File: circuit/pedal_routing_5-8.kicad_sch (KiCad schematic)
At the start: 12 parts, among them U23 CD4051B, U24 CD4051B, U25 CD4051B, U26 CD4051B

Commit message: Created pdf and made minor readabilty changes.
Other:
- title: ESP332 Guitar Patch Bay -> (none)
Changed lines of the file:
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@@
 	(generator "eeschema")
 	(generator_version "9.0")
-	(paper "USLetter")
-	(title_block
-		(title "ESP332 Guitar Patch Bay")
-		(date "2025-05-27")
-		(rev "1")
-	)
+	(paper "A4")
 	(text "Pedal 8 Routing"
 		(exclude_from_sim no)

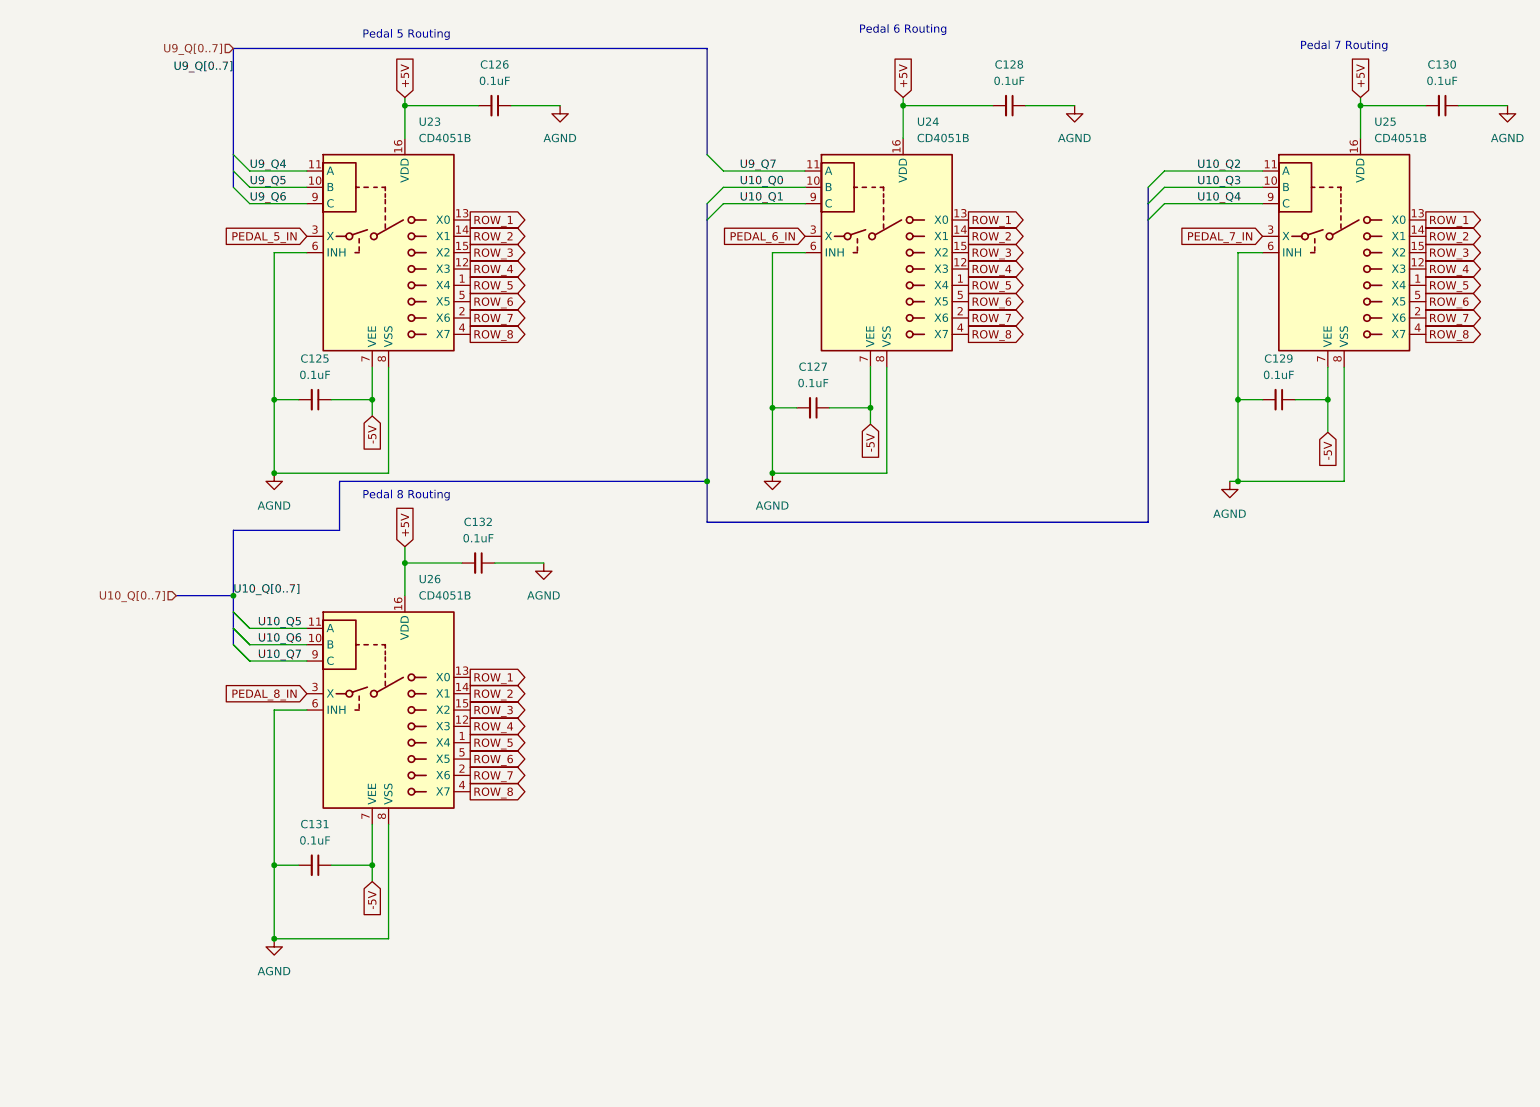
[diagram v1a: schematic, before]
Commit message: Rebuilt Matrix and added inhibit function.
Matrix was flawed, It now supports 8 FX loops (pedals) in any order. Or optionally none at all with a buffered bypass, or anywhere in between. The inhibit function will allow the option to press any loop foot switch an enable or disable it without reprogramming.
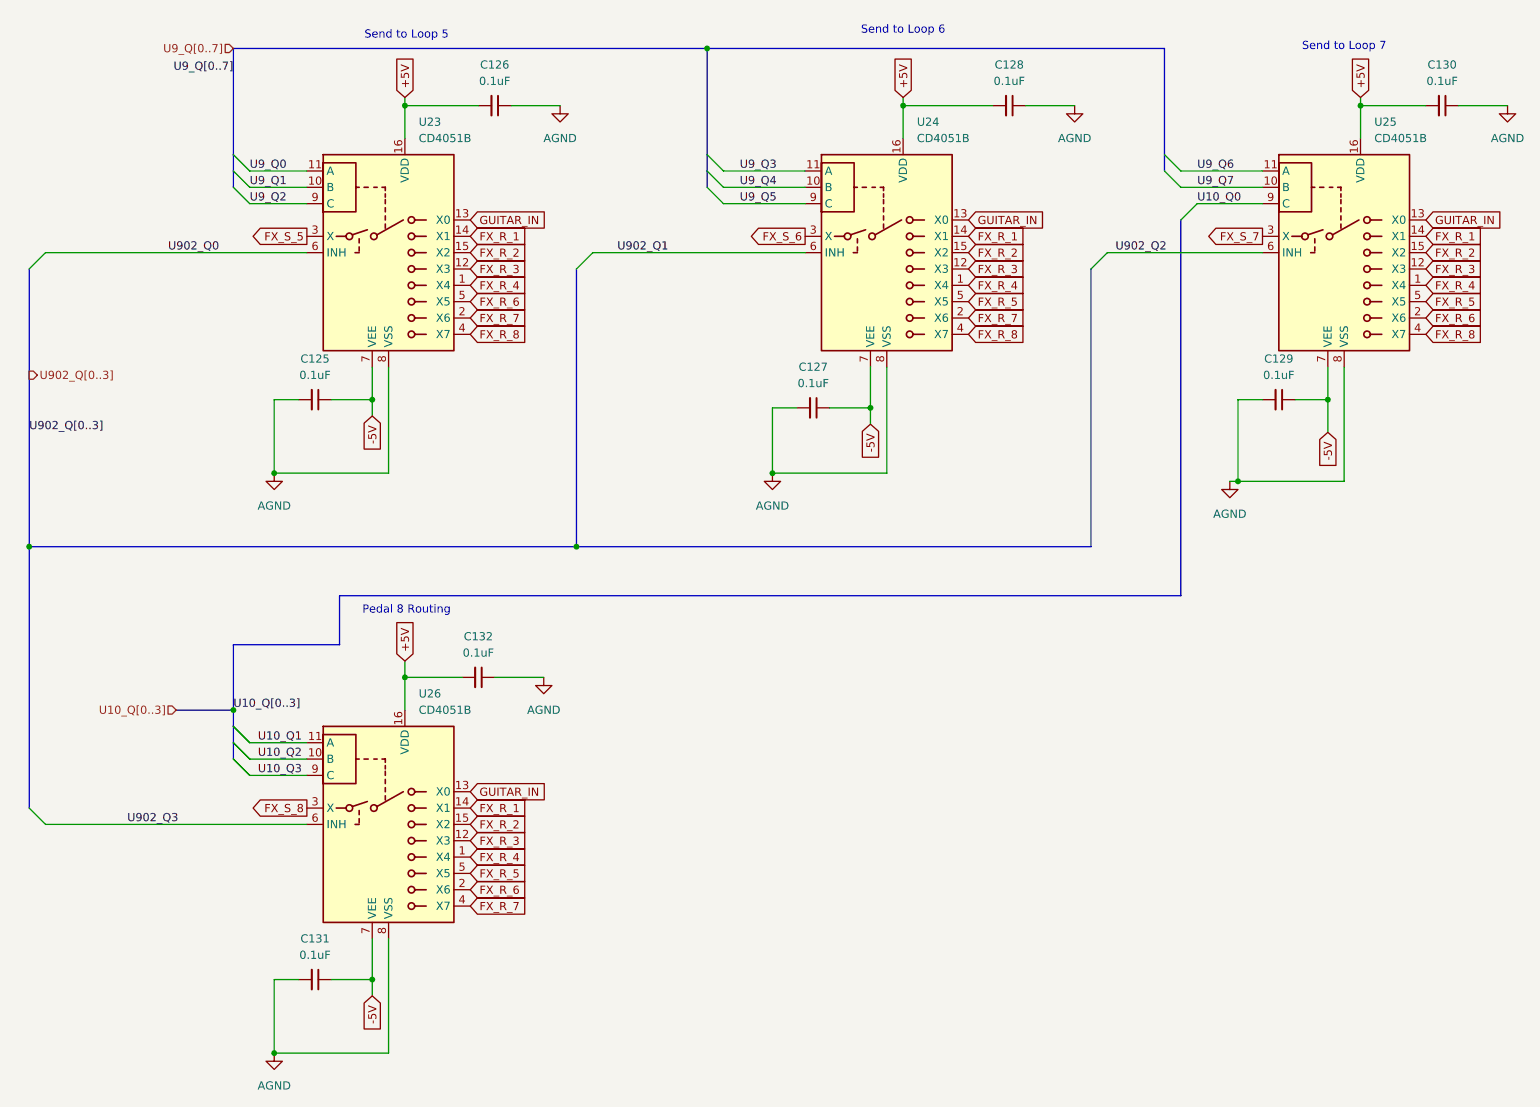
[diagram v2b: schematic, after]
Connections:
- net U10_Q4 is gone; now on net U10_Q0: U25.9 (C)
- net U10_Q5 is gone; now on net U10_Q1: U26.11 (A)
- net U10_Q6 is gone; now on net U10_Q2: U26.10 (B)
- net U10_Q7 is gone; now on net U10_Q3: U26.9 (C)
- net AGND: no longer U23.6 (INH), U24.6 (INH), U25.6 (INH), U26.6 (INH)
- net U10_Q0: no longer U24.10 (B)
- net U10_Q1: no longer U24.9 (C)
- net U10_Q2: no longer U25.11 (A)
- net U10_Q3: no longer U25.10 (B)
- net U9_Q4: now also U24.10 (B); no longer U23.11 (A)
- net U9_Q5: now also U24.9 (C); no longer U23.10 (B)
- net U9_Q6: now also U25.11 (A); no longer U23.9 (C)
- net U9_Q7: now also U25.10 (B); no longer U24.11 (A)
- net PEDAL_5_IN renamed FX_S_5
- net PEDAL_6_IN renamed FX_S_6
- net PEDAL_7_IN renamed FX_S_7
- net PEDAL_8_IN renamed FX_S_8
- net ROW_1 renamed GUITAR_IN
- net ROW_2 renamed FX_R_1
- net ROW_3 renamed FX_R_2
- net ROW_4 renamed FX_R_3
- net ROW_5 renamed FX_R_4
- net ROW_6 renamed FX_R_5
- net FX_R_5: no longer U23.5 (X5)
- net ROW_7 renamed FX_R_6
- net FX_R_6: now also U23.5 (X5); no longer U23.2 (X6), U24.2 (X6)
- net ROW_8 renamed FX_R_8
- net FX_R_8: no longer U26.4 (X7)
- new net FX_R_7: U23.2 (X6), U24.2 (X6), U26.4 (X7)
- new net U902_Q0: U23.6 (INH)
- new net U902_Q1: U24.6 (INH)
- new net U902_Q2: U25.6 (INH)
- new net U902_Q3: U26.6 (INH)
- new net U9_Q0: U23.11 (A)
- new net U9_Q1: U23.10 (B)
- new net U9_Q2: U23.9 (C)
- new net U9_Q3: U24.11 (A)
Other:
- note added: "Send to Loop 5"
- note added: "Send to Loop 6"
- note added: "Send to Loop 7"
- note removed: "Pedal 5 Routing"
- note removed: "Pedal 6 Routing"
- note removed: "Pedal 7 Routing"
- moved on the sheet: C131, C132, U26

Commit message: Re-annotation of circuit, new PCB routing, updated PDF
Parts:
- renumbered C126 to C601, C128 to C602, C130 to C603, C125 to C604, C129 to C605, C127 to C606, C132 to C607, C131 to C608, U23 to U601, U24 to U602, U25 to U603, U26 to U604
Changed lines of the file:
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@@
 		(dnp no)
 		(fields_autoplaced yes)
-		(property "Reference" "U26"
+		(property "Reference" "U604"
 			(at 77.0733 119.38 0)
 			(effects
@@
 			(project "circuit"
 				(path "/420e3d7a-6c9a-4806-b4be-05d56aeb21de/badefe61-f2aa-4ce3-b43f-f44172d96524"
-					(reference "U26")
+					(reference "U604")
 					(unit 1)
 				)
@@
 		(dnp no)
 		(fields_autoplaced yes)
-		(property "Reference" "C130"
+		(property "Reference" "C603"
 			(at 236.2136 21.59 90)
 			(effects
@@
 			(project "circuit"
 				(path "/420e3d7a-6c9a-4806-b4be-05d56aeb21de/badefe61-f2aa-4ce3-b43f-f44172d96524"
-					(reference "C130")
+					(reference "C603")
 					(unit 1)
 				)
@@
 		(on_board yes)
 		(dnp no)
-		(property "Reference" "#PWR0604"
+		(property "Reference" "#PWR0605"
 			(at 132.08 91.44 0)
 			(effects
@@
 			(project "circuit"
 				(path "/420e3d7a-6c9a-4806-b4be-05d56aeb21de/badefe61-f2aa-4ce3-b43f-f44172d96524"
-					(reference "#PWR0604")
+					(reference "#PWR0605")
 					(unit 1)
 				)
@@
 		(on_board yes)
 		(dnp no)
-		(property "Reference" "#PWR0107"
+		(property "Reference" "#PWR0602"
 			(at 179.07 34.29 0)
 			(effects
@@
 			(project "circuit"
 				(path "/420e3d7a-6c9a-4806-b4be-05d56aeb21de/badefe61-f2aa-4ce3-b43f-f44172d96524"
-					(reference "#PWR0107")
+					(reference "#PWR0602")
 					(unit 1)
 				)
@@
 		(dnp no)
 		(fields_autoplaced yes)
-		(property "Reference" "C129"
+		(property "Reference" "C605"
 			(at 210.8136 67.31 90)
 			(effects
@@
 			(project "circuit"
 				(path "/420e3d7a-6c9a-4806-b4be-05d56aeb21de/badefe61-f2aa-4ce3-b43f-f44172d96524"
-					(reference "C129")
+					(reference "C605")
 					(unit 1)
 				)
@@
 		(on_board yes)
 		(dnp no)
-		(property "Reference" "#PWR0601"
+		(property "Reference" "#PWR0604"
 			(at 54.61 91.44 0)
 			(effects
@@
 			(project "circuit"
 				(path "/420e3d7a-6c9a-4806-b4be-05d56aeb21de/badefe61-f2aa-4ce3-b43f-f44172d96524"
-					(reference "#PWR0601")
+					(reference "#PWR0604")
 					(unit 1)
 				)
@@
 		(on_board yes)
 		(dnp no)
-		(property "Reference" "#PWR0106"
+		(property "Reference" "#PWR0601"
 			(at 99.06 34.29 0)
 			(effects
@@
 			(project "circuit"
 				(path "/420e3d7a-6c9a-4806-b4be-05d56aeb21de/badefe61-f2aa-4ce3-b43f-f44172d96524"
-					(reference "#PWR0106")
+					(reference "#PWR0601")
 					(unit 1)
 				)
@@
 		(dnp no)
 		(fields_autoplaced yes)
-		(property "Reference" "C132"
+		(property "Reference" "C607"
 			(at 86.3536 110.49 90)
 			(effects
@@
 			(project "circuit"
 				(path "/420e3d7a-6c9a-4806-b4be-05d56aeb21de/badefe61-f2aa-4ce3-b43f-f44172d96524"
-					(reference "C132")
+					(reference "C607")
 					(unit 1)
 				)
@@
 		(dnp no)
 		(fields_autoplaced yes)
-		(property "Reference" "C131"
+		(property "Reference" "C608"
 			(at 60.9536 157.48 90)
 			(effects
@@
 			(project "circuit"
 				(path "/420e3d7a-6c9a-4806-b4be-05d56aeb21de/badefe61-f2aa-4ce3-b43f-f44172d96524"
-					(reference "C131")
+					(reference "C608")
 					(unit 1)
 				)
@@
 		(dnp no)
 		(fields_autoplaced yes)
-		(property "Reference" "C127"
+		(property "Reference" "C606"
 			(at 138.4236 68.58 90)
 			(effects
@@
 			(project "circuit"
 				(path "/420e3d7a-6c9a-4806-b4be-05d56aeb21de/badefe61-f2aa-4ce3-b43f-f44172d96524"
-					(reference "C127")
+					(reference "C606")
 					(unit 1)
 				)
@@
 		(on_board yes)
 		(dnp no)
-		(property "Reference" "#PWR0108"
+		(property "Reference" "#PWR0603"
 			(at 246.38 34.29 0)
 			(effects
@@
 			(project "circuit"
 				(path "/420e3d7a-6c9a-4806-b4be-05d56aeb21de/badefe61-f2aa-4ce3-b43f-f44172d96524"
-					(reference "#PWR0108")
+					(reference "#PWR0603")
 					(unit 1)
 				)
@@
 		(dnp no)
 		(fields_autoplaced yes)
-		(property "Reference" "C126"
+		(property "Reference" "C601"
 			(at 88.8936 21.59 90)
 			(effects
@@
 			(project "circuit"
 				(path "/420e3d7a-6c9a-4806-b4be-05d56aeb21de/badefe61-f2aa-4ce3-b43f-f44172d96524"
-					(reference "C126")
+					(reference "C601")
 					(unit 1)
 				)
@@
 		(on_board yes)
 		(dnp no)
-		(property "Reference" "#PWR0603"
+		(property "Reference" "#PWR0606"
 			(at 203.2 92.71 0)
 			(effects
@@
 			(project "circuit"
 				(path "/420e3d7a-6c9a-4806-b4be-05d56aeb21de/badefe61-f2aa-4ce3-b43f-f44172d96524"
-					(reference "#PWR0603")
+					(reference "#PWR0606")
 					(unit 1)
 				)
@@
 		(dnp no)
 		(fields_autoplaced yes)
-		(property "Reference" "C128"
+		(property "Reference" "C602"
 			(at 168.9036 21.59 90)
 			(effects
@@
 			(project "circuit"
 				(path "/420e3d7a-6c9a-4806-b4be-05d56aeb21de/badefe61-f2aa-4ce3-b43f-f44172d96524"
-					(reference "C128")
+					(reference "C602")
 					(unit 1)
 				)
@@
 		(dnp no)
 		(fields_autoplaced yes)
-		(property "Reference" "U23"
+		(property "Reference" "U601"
 			(at 77.0733 30.48 0)
 			(effects
@@
 			(project "circuit"
 				(path "/420e3d7a-6c9a-4806-b4be-05d56aeb21de/badefe61-f2aa-4ce3-b43f-f44172d96524"
-					(reference "U23")
+					(reference "U601")
 					(unit 1)
 				)
@@
 		(dnp no)
 		(fields_autoplaced yes)
-		(property "Reference" "C125"
+		(property "Reference" "C604"
 			(at 60.9536 67.31 90)
 			(effects
@@
 			(project ""
 				(path "/420e3d7a-6c9a-4806-b4be-05d56aeb21de/badefe61-f2aa-4ce3-b43f-f44172d96524"
-					(reference "C125")
+					(reference "C604")
 					(unit 1)
 				)
@@
 		(on_board yes)
 		(dnp no)
-		(property "Reference" "#PWR0602"
+		(property "Reference" "#PWR0608"
 			(at 54.61 181.61 0)
 			(effects
@@
 			(project "circuit"
 				(path "/420e3d7a-6c9a-4806-b4be-05d56aeb21de/badefe61-f2aa-4ce3-b43f-f44172d96524"
-					(reference "#PWR0602")
+					(reference "#PWR0608")
 					(unit 1)
 				)
@@
 		(dnp no)
 		(fields_autoplaced yes)
-		(property "Reference" "U24"
+		(property "Reference" "U602"
 			(at 154.5433 30.48 0)
 			(effects
@@
 			(project "circuit"
 				(path "/420e3d7a-6c9a-4806-b4be-05d56aeb21de/badefe61-f2aa-4ce3-b43f-f44172d96524"
-					(reference "U24")
+					(reference "U602")
 					(unit 1)
 				)
@@
 		(dnp no)
 		(fields_autoplaced yes)
-		(property "Reference" "U25"
+		(property "Reference" "U603"
 			(at 225.6633 30.48 0)
 			(effects
@@
 			(project "circuit"
 				(path "/420e3d7a-6c9a-4806-b4be-05d56aeb21de/badefe61-f2aa-4ce3-b43f-f44172d96524"
-					(reference "U25")
+					(reference "U603")
 					(unit 1)
 				)
@@
 		(on_board yes)
 		(dnp no)
-		(property "Reference" "#PWR0109"
+		(property "Reference" "#PWR0607"
 			(at 96.52 123.19 0)
 			(effects
@@
 			(project "circuit"
 				(path "/420e3d7a-6c9a-4806-b4be-05d56aeb21de/badefe61-f2aa-4ce3-b43f-f44172d96524"
-					(reference "#PWR0109")
-					(unit 1)
-				)
+					(reference "#PWR0607")
+					(unit 1)
+				)
